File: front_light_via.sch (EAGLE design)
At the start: 9 parts

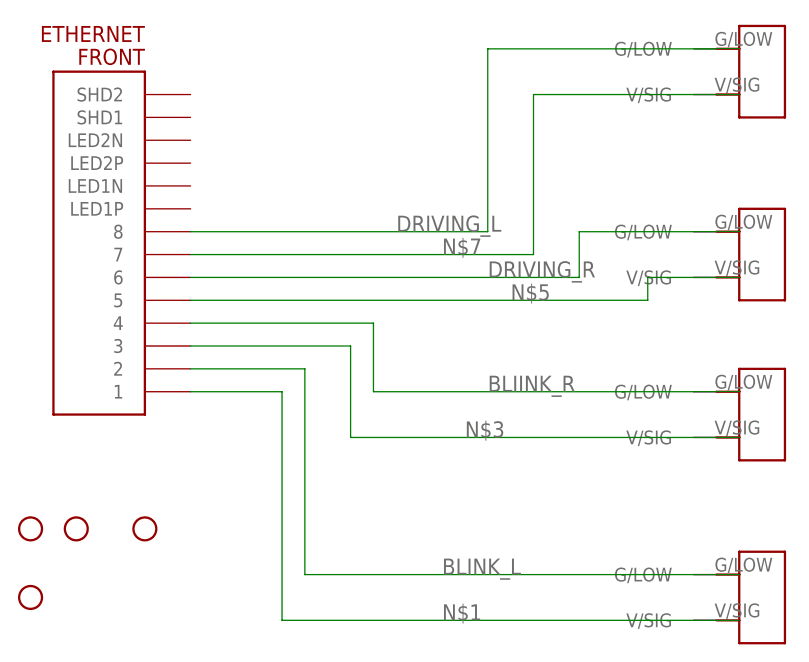
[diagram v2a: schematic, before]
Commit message: correct all routing errors
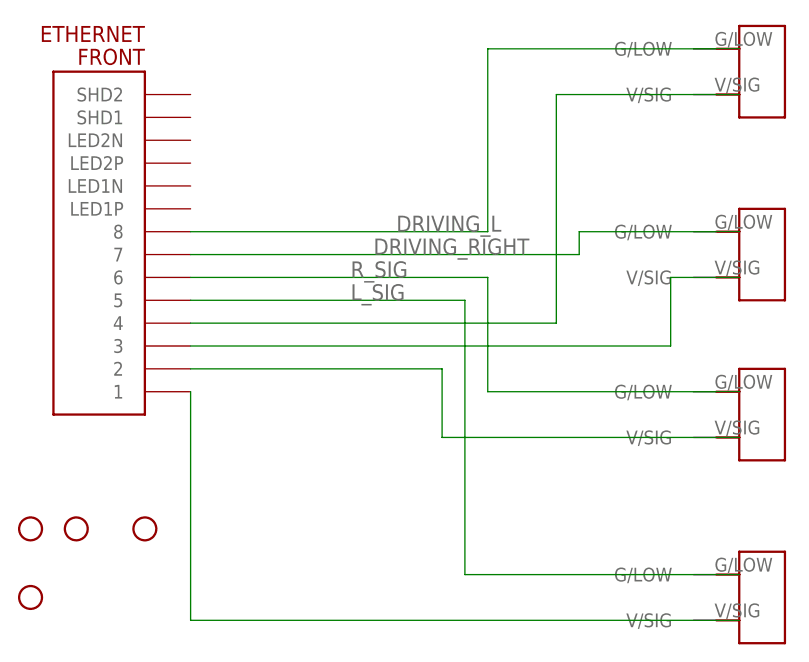
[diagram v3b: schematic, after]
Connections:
- removed net BLIINK_R: FRONT.4, U$3.G/LOW
- removed net BLINK_L: FRONT.2, U$4.G/LOW
- removed net DRIVING_R: FRONT.6, U$2.G/LOW
- removed net N$3: FRONT.3, U$3.V/SIG
- removed net N$7 (its old number): FRONT.7, U$1.V/SIG
- new net DRIVING_RIGHT: FRONT.7, U$2.G/LOW
- new net L_SIG: FRONT.5, U$4.G/LOW
- new net N$4: FRONT.4, U$1.V/SIG
- new net N$6: FRONT.2, U$3.V/SIG
- new net R_SIG: FRONT.6, U$3.G/LOW
- net N$5: now also FRONT.3; no longer FRONT.5
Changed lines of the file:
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@@
 <?xml version="1.0" encoding="utf-8"?>
 <!DOCTYPE eagle SYSTEM "eagle.dtd">
-<eagle version="8.6.1">
+<eagle version="9.0.0">
 <drawing>
 <settings>
@@
 </busses>
 <nets>
-<net name="N$1" class="0">
-<segment>
-<pinref part="FRONT" gate="G$1" pin="1"/>
-<wire x1="53.34" y1="53.34" x2="63.5" y2="53.34" width="0.1524" layer="91"/>
-<wire x1="63.5" y1="53.34" x2="63.5" y2="27.94" width="0.1524" layer="91"/>
-<wire x1="63.5" y1="27.94" x2="114.3" y2="27.94" width="0.1524" layer="91"/>
-<label x="81.28" y="27.94" size="1.778" layer="95"/>
-<pinref part="U$4" gate="G$1" pin="V/SIG"/>
-</segment>
-</net>
-<net name="BLINK_L" class="0">
-<segment>
-<pinref part="FRONT" gate="G$1" pin="2"/>
-<wire x1="53.34" y1="55.88" x2="66.04" y2="55.88" width="0.1524" layer="91"/>
-<wire x1="66.04" y1="55.88" x2="66.04" y2="33.02" width="0.1524" layer="91"/>
-<wire x1="66.04" y1="33.02" x2="114.3" y2="33.02" width="0.1524" layer="91"/>
-<label x="81.28" y="33.02" size="1.778" layer="95"/>
-<pinref part="U$4" gate="G$1" pin="G/LOW"/>
-</segment>
-</net>
-<net name="N$3" class="0">
-<segment>
-<pinref part="FRONT" gate="G$1" pin="3"/>
-<wire x1="53.34" y1="58.42" x2="71.12" y2="58.42" width="0.1524" layer="91"/>
-<wire x1="71.12" y1="58.42" x2="71.12" y2="48.26" width="0.1524" layer="91"/>
-<wire x1="71.12" y1="48.26" x2="114.3" y2="48.26" width="0.1524" layer="91"/>
-<label x="83.82" y="48.26" size="1.778" layer="95"/>
-<pinref part="U$3" gate="G$1" pin="V/SIG"/>
-</segment>
-</net>
-<net name="BLIINK_R" class="0">
-<segment>
-<pinref part="FRONT" gate="G$1" pin="4"/>
-<wire x1="53.34" y1="60.96" x2="73.66" y2="60.96" width="0.1524" layer="91"/>
-<wire x1="73.66" y1="60.96" x2="73.66" y2="53.34" width="0.1524" layer="91"/>
-<wire x1="73.66" y1="53.34" x2="114.3" y2="53.34" width="0.1524" layer="91"/>
-<label x="86.36" y="53.34" size="1.778" layer="95"/>
-<pinref part="U$3" gate="G$1" pin="G/LOW"/>
-</segment>
-</net>
-<net name="N$5" class="0">
-<segment>
-<pinref part="FRONT" gate="G$1" pin="5"/>
-<wire x1="53.34" y1="63.5" x2="104.14" y2="63.5" width="0.1524" layer="91"/>
-<wire x1="104.14" y1="63.5" x2="104.14" y2="66.04" width="0.1524" layer="91"/>
-<wire x1="104.14" y1="66.04" x2="114.3" y2="66.04" width="0.1524" layer="91"/>
-<label x="88.9" y="63.5" size="1.778" layer="95"/>
-<pinref part="U$2" gate="G$1" pin="V/SIG"/>
-</segment>
-</net>
-<net name="DRIVING_R" class="0">
-<segment>
-<pinref part="FRONT" gate="G$1" pin="6"/>
-<wire x1="53.34" y1="66.04" x2="96.52" y2="66.04" width="0.1524" layer="91"/>
-<wire x1="96.52" y1="66.04" x2="96.52" y2="71.12" width="0.1524" layer="91"/>
-<wire x1="96.52" y1="71.12" x2="114.3" y2="71.12" width="0.1524" layer="91"/>
-<label x="86.36" y="66.04" size="1.778" layer="95"/>
-<pinref part="U$2" gate="G$1" pin="G/LOW"/>
-</segment>
-</net>
-<net name="N$7" class="0">
-<segment>
-<pinref part="FRONT" gate="G$1" pin="7"/>
-<wire x1="53.34" y1="68.58" x2="91.44" y2="68.58" width="0.1524" layer="91"/>
-<wire x1="91.44" y1="68.58" x2="91.44" y2="86.36" width="0.1524" layer="91"/>
-<wire x1="114.3" y1="86.36" x2="91.44" y2="86.36" width="0.1524" layer="91"/>
-<label x="81.28" y="68.58" size="1.778" layer="95"/>
-<pinref part="U$1" gate="G$1" pin="V/SIG"/>
-</segment>
-</net>
 <net name="DRIVING_L" class="0">
 <segment>
@@
 </segment>
 </net>
+<net name="DRIVING_RIGHT" class="0">
+<segment>
+<pinref part="FRONT" gate="G$1" pin="7"/>
+<wire x1="53.34" y1="68.58" x2="96.52" y2="68.58" width="0.1524" layer="91"/>
+<wire x1="96.52" y1="68.58" x2="96.52" y2="71.12" width="0.1524" layer="91"/>
+<pinref part="U$2" gate="G$1" pin="G/LOW"/>
+<wire x1="96.52" y1="71.12" x2="114.3" y2="71.12" width="0.1524" layer="91"/>
+<label x="73.66" y="68.58" size="1.778" layer="95"/>
+</segment>
+</net>
+<net name="R_SIG" class="0">
+<segment>
+<pinref part="U$3" gate="G$1" pin="G/LOW"/>
+<wire x1="114.3" y1="53.34" x2="86.36" y2="53.34" width="0.1524" layer="91"/>
+<wire x1="86.36" y1="53.34" x2="86.36" y2="66.04" width="0.1524" layer="91"/>
+<pinref part="FRONT" gate="G$1" pin="6"/>
+<wire x1="86.36" y1="66.04" x2="53.34" y2="66.04" width="0.1524" layer="91"/>
+<label x="71.12" y="66.04" size="1.778" layer="95"/>
+</segment>
+</net>
+<net name="L_SIG" class="0">
+<segment>
+<pinref part="U$4" gate="G$1" pin="G/LOW"/>
+<wire x1="114.3" y1="33.02" x2="83.82" y2="33.02" width="0.1524" layer="91"/>
+<wire x1="83.82" y1="33.02" x2="83.82" y2="63.5" width="0.1524" layer="91"/>
+<pinref part="FRONT" gate="G$1" pin="5"/>
+<wire x1="83.82" y1="63.5" x2="53.34" y2="63.5" width="0.1524" layer="91"/>
+<label x="71.12" y="63.5" size="1.778" layer="95"/>
+</segment>
+</net>
+<net name="N$4" class="0">
+<segment>
+<pinref part="FRONT" gate="G$1" pin="4"/>
+<wire x1="53.34" y1="60.96" x2="93.98" y2="60.96" width="0.1524" layer="91"/>
+<wire x1="93.98" y1="60.96" x2="93.98" y2="86.36" width="0.1524" layer="91"/>
+<pinref part="U$1" gate="G$1" pin="V/SIG"/>
+<wire x1="93.98" y1="86.36" x2="114.3" y2="86.36" width="0.1524" layer="91"/>
+</segment>
+</net>
+<net name="N$5" class="0">
+<segment>
+<pinref part="FRONT" gate="G$1" pin="3"/>
+<wire x1="53.34" y1="58.42" x2="106.68" y2="58.42" width="0.1524" layer="91"/>
+<wire x1="106.68" y1="58.42" x2="106.68" y2="66.04" width="0.1524" layer="91"/>
+<pinref part="U$2" gate="G$1" pin="V/SIG"/>
+<wire x1="106.68" y1="66.04" x2="114.3" y2="66.04" width="0.1524" layer="91"/>
+</segment>
+</net>
+<net name="N$6" class="0">
+<segment>
+<pinref part="FRONT" gate="G$1" pin="2"/>
+<wire x1="53.34" y1="55.88" x2="81.28" y2="55.88" width="0.1524" layer="91"/>
+<wire x1="81.28" y1="55.88" x2="81.28" y2="48.26" width="0.1524" layer="91"/>
+<pinref part="U$3" gate="G$1" pin="V/SIG"/>
+<wire x1="81.28" y1="48.26" x2="114.3" y2="48.26" width="0.1524" layer="91"/>
+</segment>
+</net>
+<net name="N$7" class="0">
+<segment>
+<pinref part="FRONT" gate="G$1" pin="1"/>
+<pinref part="U$4" gate="G$1" pin="V/SIG"/>
+<wire x1="53.34" y1="53.34" x2="53.34" y2="27.94" width="0.1524" layer="91"/>
+<wire x1="53.34" y1="27.94" x2="114.3" y2="27.94" width="0.1524" layer="91"/>
+</segment>
+</net>
